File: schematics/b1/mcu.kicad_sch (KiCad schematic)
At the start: 0 parts

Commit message: Added schematic page for the status block.
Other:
- company: (none) -> shawnd.xyz
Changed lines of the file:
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@@
   (title_block
     (title "B1")
-    (date "2024-02-01")
+    (date "2024-02-05")
     (rev "1")
+    (company "shawnd.xyz")
     (comment 2 "scanning as well as radio communications and outputs/displays.")
     (comment 3 "A B1 (Badger One) node is the core hardware unit of the Badger sytem. It handles card")

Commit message: General schematic updates.
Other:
- title: B1 -> (none)
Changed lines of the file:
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@@
   (paper "A4")
   (title_block
-    (title "B1")
     (date "2024-02-06")
     (rev "1")
     (company "shawnd.xyz")
-    (comment 2 "scanning as well as radio communications and outputs/displays.")
-    (comment 3 "A B1 (Badger One) node is the core hardware unit of the Badger sytem. It handles card")
   )
 )

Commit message: Added MCU primary schematic page.
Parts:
- added C17, C19: 22pF, Capacitor_THT:C_Disc_D3.0mm_W1.6mm_P2.50mm, symbol Device:C
- added C21: 0.1u, symbol Device:C
- added C22: 1u, symbol Device:C
- added C23: 10u, symbol Device:C_Polarized
- added Q10, Q11, Q12: 2N3904, Package_TO_SOT_THT:TO-92_Inline, symbol Transistor_BJT:2N3904
- added R31: 10kΩ, Resistor_THT:R_Axial_DIN0204_L3.6mm_D1.6mm_P7.62mm_Horizontal, symbol Device:R
- added R32, R33, R34, R35, R36, R37: 10k, symbol Device:R
- added U9: ATmega328-P, Package_DIP:DIP-28_W7.62mm_Socket, symbol MCU_Microchip_ATmega:ATmega328-P
- added Y1: 16MHz, Crystal:Crystal_HC49-U_Vertical, symbol Device:Crystal
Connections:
- new net: Q10.2 (B), R32.2
- new net: Q11.2 (B), R34.2
- new net: C19.1, U9.10 (XTAL2/PB7), Y1.1
- new net: R31.2, U9.1 (~{RESET}/PC6)
- new net: C17.2, U9.9 (XTAL1/PB6), Y1.2
- new net: Q12.2 (B), R37.2
- new net DIO0: U9.12 (PD6)
- new net GND: C17.1, C19.2, C21.2, C22.2, C23.2, Q10.1 (E), Q11.1 (E), Q12.1 (E), U9.22 (GND), U9.8 (GND)
- new net MISO: U9.18 (PB4)
- new net MOSI: U9.17 (PB3)
- new net RST0: U9.6 (PD4)
- new net SCK: U9.19 (PB5)
- new net TONE: U9.23 (PC0)
- new net VCC: C21.1, C22.1, C23.1, R31.1, R33.2, R35.2, R36.2, U9.20 (AVCC), U9.7 (VCC)
- new net VCC_ISR: Q10.3 (C), R33.1
- new net VCC_LORA: Q12.3 (C), R36.1
- new net VCC_SCAN: Q11.3 (C), R35.1
- new net ~{CS0}: R32.1, U9.16 (PB2)
- new net ~{CS1}: U9.15 (PB1)
- new net ~{CS2}: R34.1, U9.14 (PB0)
- new net ~{CS3}: R37.1, U9.13 (PD7)
- new net ~{PL}: U9.11 (PD5)
- new net ~{RST1}: U9.5 (PD3)
- no-connect marks 0 -> 3

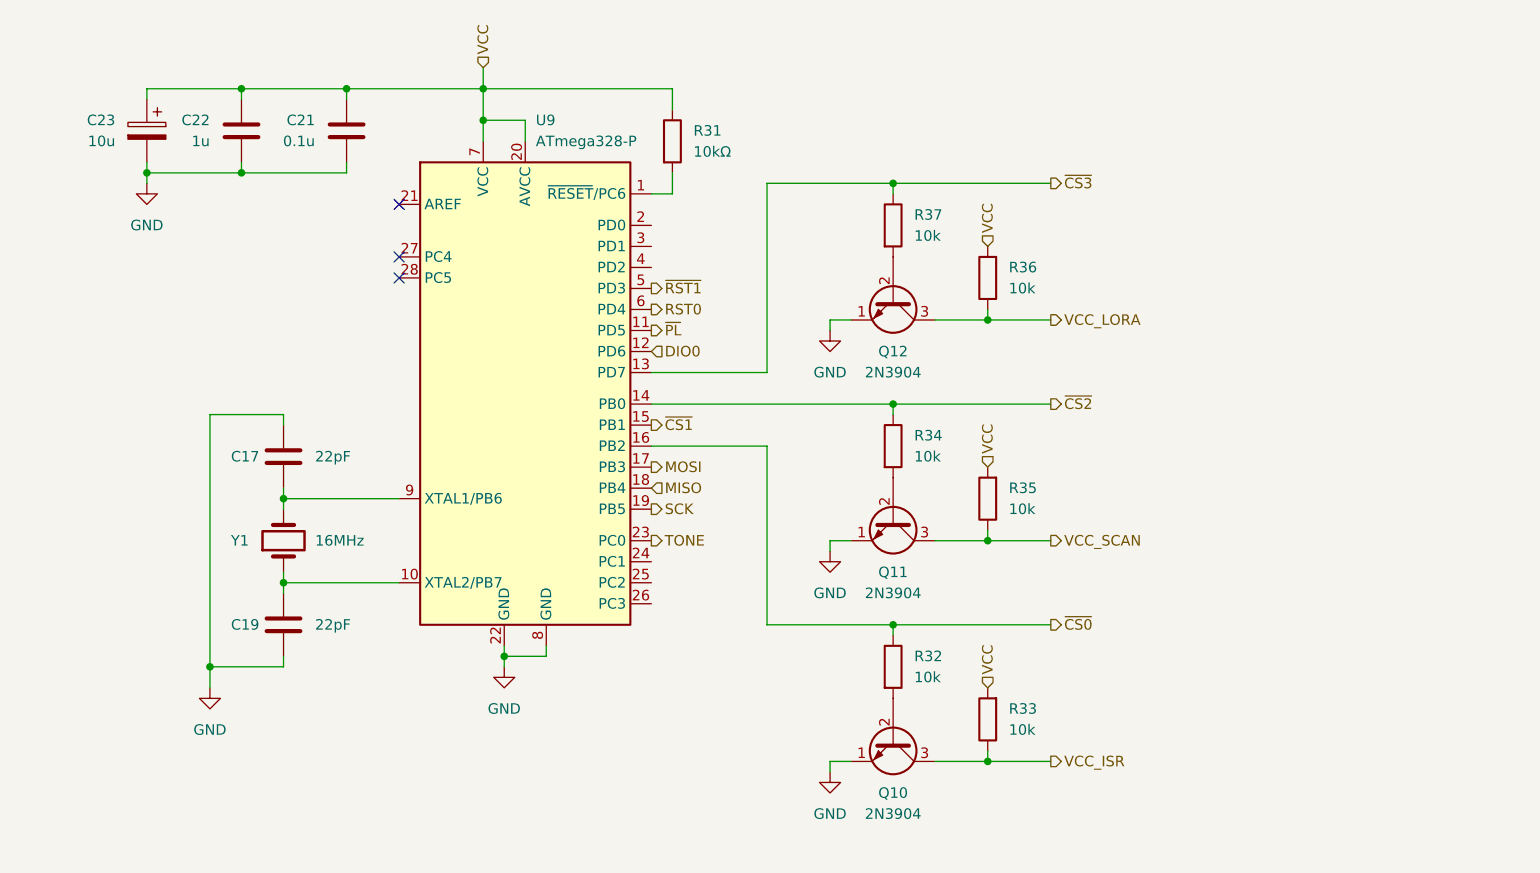
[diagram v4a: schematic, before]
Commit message: Updated MCU and B1 schematic pages.
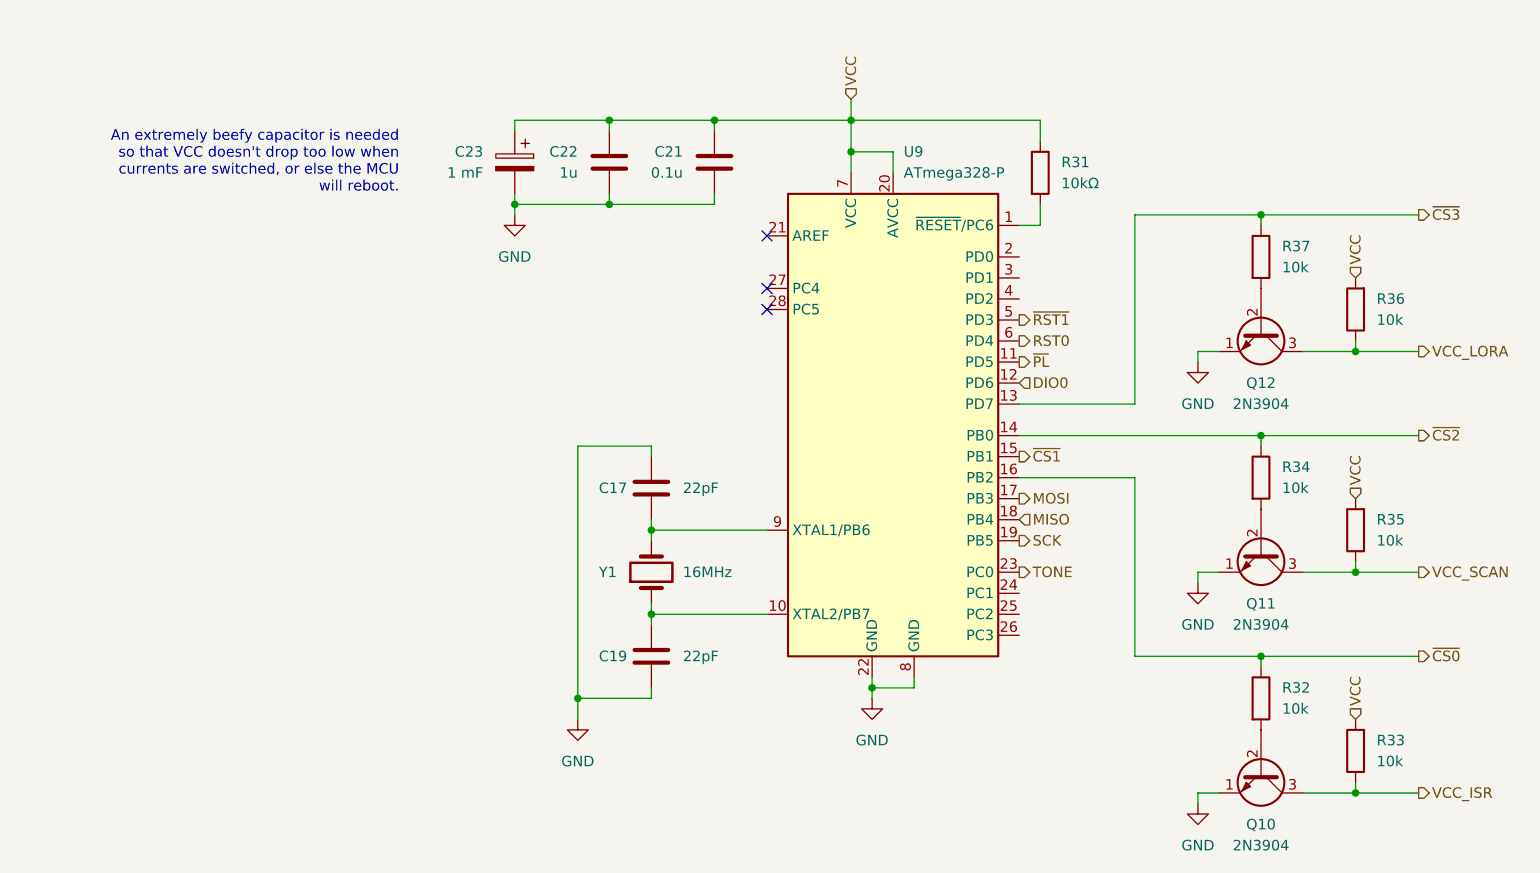
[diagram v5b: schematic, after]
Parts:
- C23: value 10u -> 1 mF
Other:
- note added: "An extremely beefy capacitor is needed so that VCC doesn't drop too low when currents are switched, or else the MCU will reboot."
- moved on the sheet: C17, C19, C21, C22, C23, Q10, Q11, Q12, R31, R32, R33, R34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

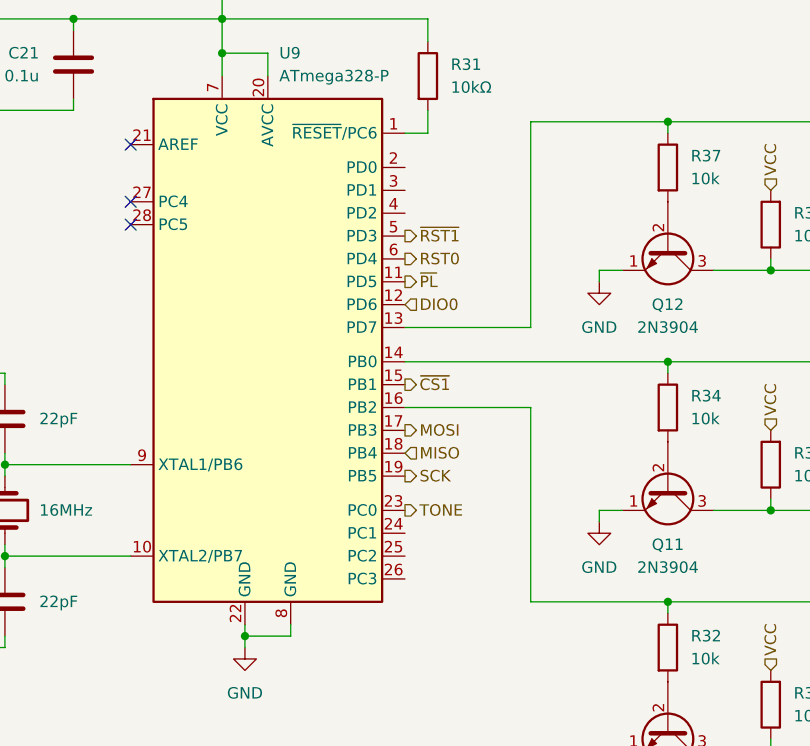
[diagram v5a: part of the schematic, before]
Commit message: Updated MCU and B1 schematics.
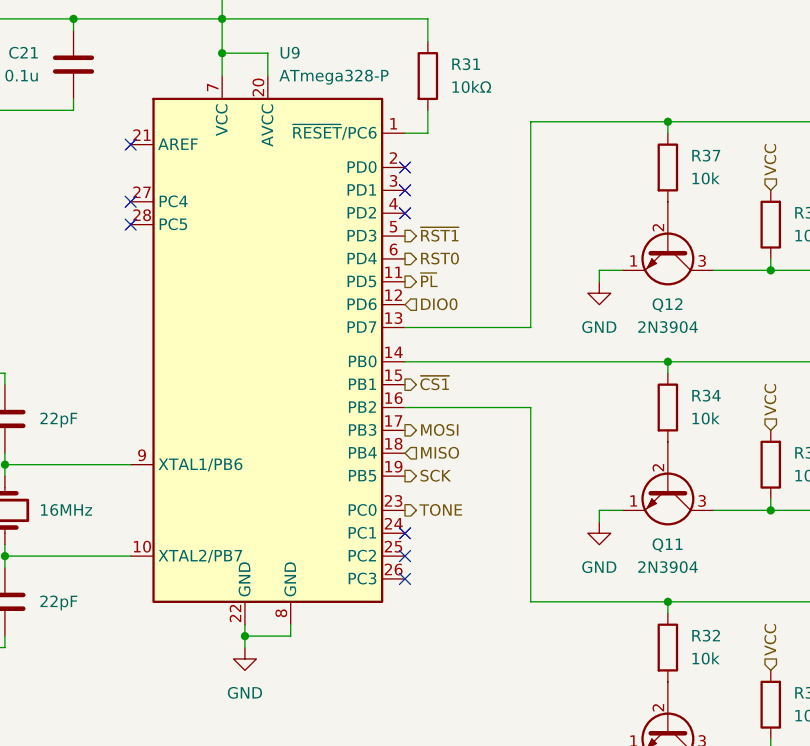
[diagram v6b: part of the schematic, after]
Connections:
- no-connect marks 3 -> 9
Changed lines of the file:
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@@
   )
   (no_connect (at 128.27 59.69))
+  (no_connect (at 158.75 107.95))
+  (no_connect (at 158.75 105.41))
+  (no_connect (at 158.75 102.87))
   (no_connect (at 128.27 68.58))
+  (no_connect (at 158.75 62.23))
+  (no_connect (at 158.75 67.31))
   (no_connect (at 128.27 66.04))
+  (no_connect (at 158.75 64.77))
   (wire (pts (xy 161.29 58.42) (xy 161.29 55.88))
     (stroke (width 0) (type default))

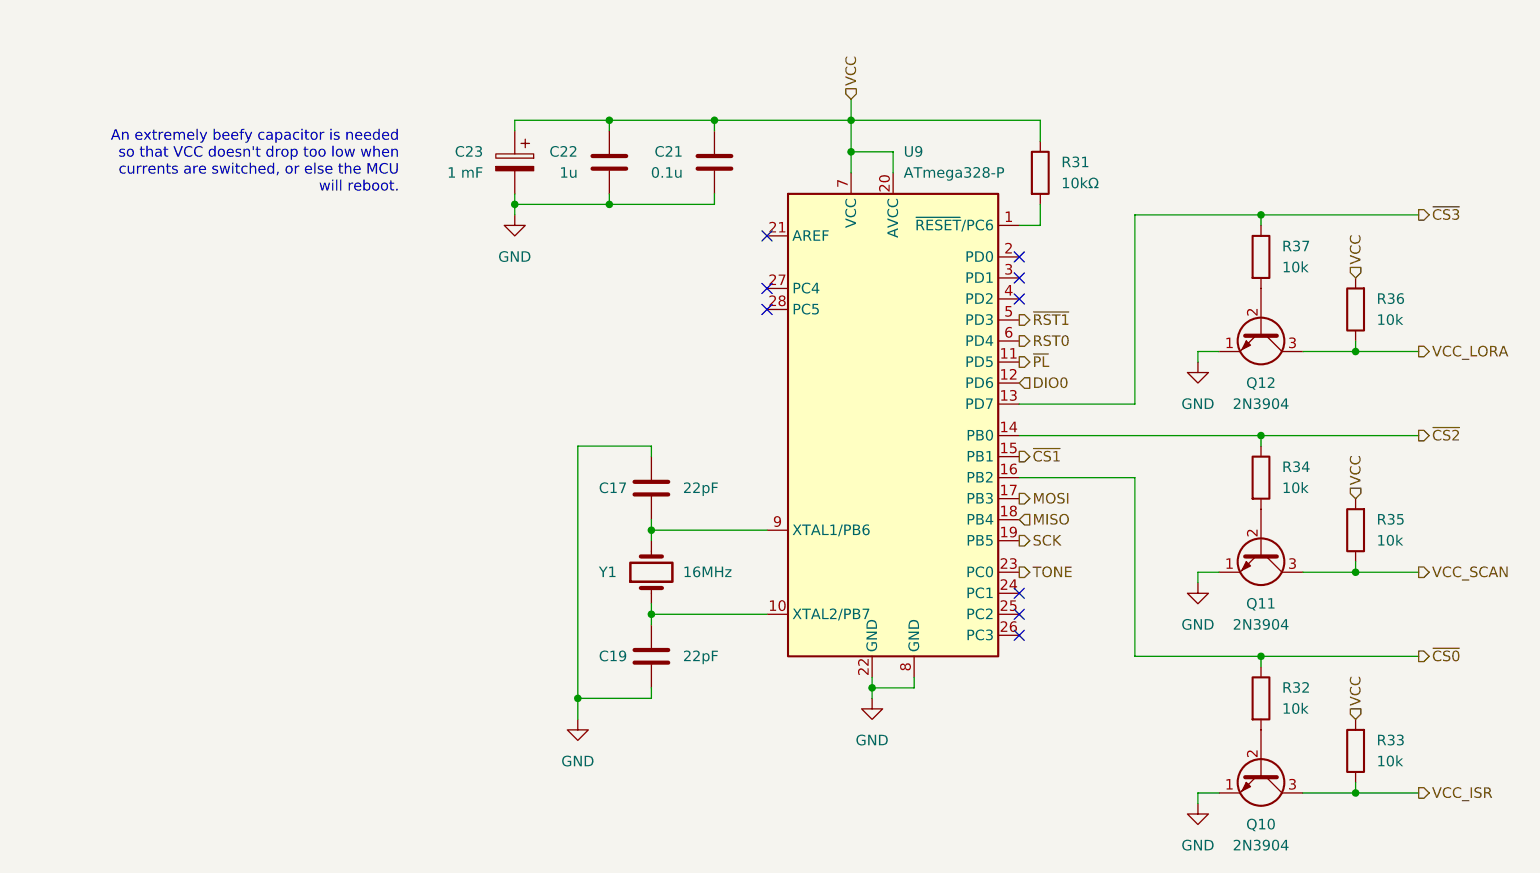
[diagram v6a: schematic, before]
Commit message: Changed tone pin.
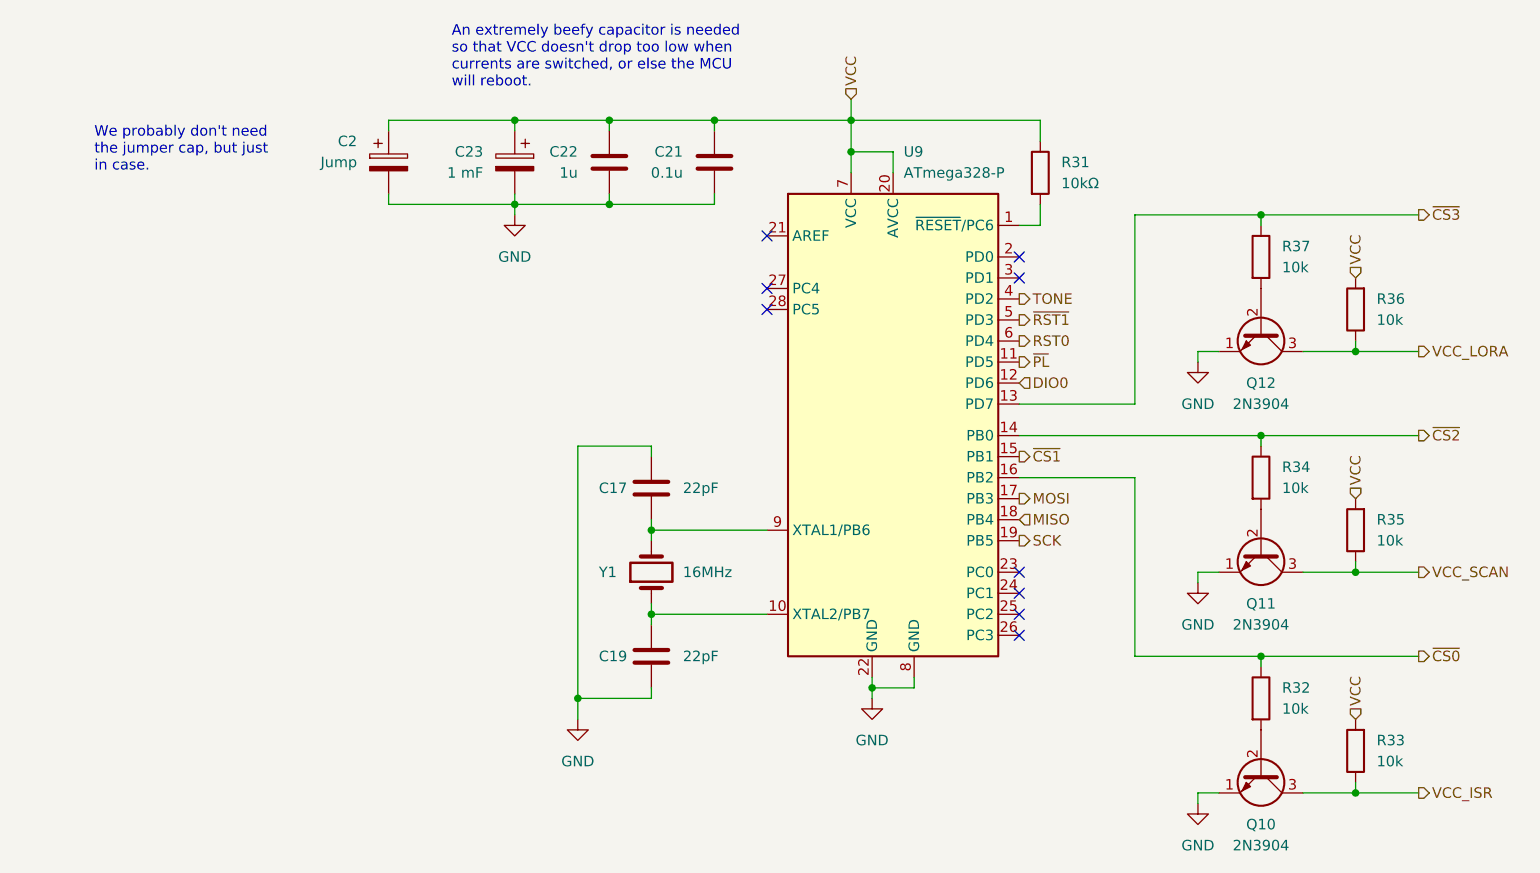
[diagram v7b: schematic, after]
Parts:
- added C2: Jump, symbol Device:C_Polarized
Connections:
- net GND: now also C2.2
- net TONE: now also U9.4 (PD2); no longer U9.23 (PC0)
- net VCC: now also C2.1
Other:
- note added: "We probably don't need the jumper cap, but just in case."
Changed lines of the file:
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@@
   (junction (at 109.22 55.88) (diameter 0) (color 0 0 0 0)
+  )
+  (junction (at 97.79 45.72) (diameter 0) (color 0 0 0 0)
   )
   (junction (at 140.97 114.3) (diameter 0) (color 0 0 0 0)
@@
   (no_connect (at 158.75 105.41))
   (no_connect (at 158.75 102.87))
+  (no_connect (at 158.75 100.33))
   (no_connect (at 128.27 68.58))
   (no_connect (at 158.75 62.23))
-  (no_connect (at 158.75 67.31))
   (no_connect (at 128.27 66.04))
   (no_connect (at 158.75 64.77))
+  (wire (pts (xy 82.55 55.88) (xy 82.55 54.61))
+    (stroke (width 0) (type default))
+  )
   (wire (pts (xy 161.29 58.42) (xy 161.29 55.88))
     (stroke (width 0) (type default))
@@
     (stroke (width 0) (type default))
   )
+  (wire (pts (xy 97.79 54.61) (xy 97.79 55.88))
+    (stroke (width 0) (type default))
+  )
   (wire (pts (xy 182.88 127) (xy 180.34 127))
     (stroke (width 0) (type default))
@@
     (stroke (width 0) (type default))
   )
-  (wire (pts (xy 97.79 54.61) (xy 97.79 55.88))
-    (stroke (width 0) (type default))
-  )
   (wire (pts (xy 121.92 45.72) (xy 138.43 45.72))
     (stroke (width 0) (type default))
   )
+  (wire (pts (xy 97.79 45.72) (xy 82.55 45.72))
+    (stroke (width 0) (type default))
+  )
   (wire (pts (xy 109.22 46.99) (xy 109.22 45.72))
     (stroke (width 0) (type default))
@@
     (stroke (width 0) (type default))
   )
+  (wire (pts (xy 82.55 55.88) (xy 97.79 55.88))
+    (stroke (width 0) (type default))
+  )
   (wire (pts (xy 199.39 99.06) (xy 199.39 100.33))
     (stroke (width 0) (type default))
@@
     (stroke (width 0) (type default))
   )
+  (wire (pts (xy 82.55 45.72) (xy 82.55 46.99))
+    (stroke (width 0) (type default))
+  )
   (wire (pts (xy 207.01 127) (xy 199.39 127))
     (stroke (width 0) (type default))
@@
   )
   (text "An extremely beefy capacitor is needed\nso that VCC doesn't drop too low when\ncurrents are switched, or else the MCU\nwill reboot."
-    (at 83.82 54.61 0)
-    (effects (font (size 1.27 1.27)) (justify right bottom))
-  )
-  (hierarchical_label "TONE" (shape output) (at 158.75 100.33 0) (fields_autoplaced)
-    (effects (font (size 1.27 1.27)) (justify left))
+    (at 90.17 41.91 0)
+    (effects (font (size 1.27 1.27)) (justify left bottom))
+  )
+  (text "We probably don't need\nthe jumper cap, but just\nin case."
+    (at 46.99 52.07 0)
+    (effects (font (size 1.27 1.27)) (justify left bottom))
   )
   (hierarchical_label "DIO0" (shape input) (at 158.75 77.47 0) (fields_autoplaced)
@@
   )
   (hierarchical_label "VCC" (shape input) (at 199.39 64.77 90) (fields_autoplaced)
+    (effects (font (size 1.27 1.27)) (justify left))
+  )
+  (hierarchical_label "TONE" (shape output) (at 158.75 67.31 0) (fields_autoplaced)
     (effects (font (size 1.27 1.27)) (justify left))
   )
@@
         )
       )
+    )
+  )
+  (symbol (lib_id "Device:C_Polarized") (at 82.55 50.8 0) (unit 1)
+    (in_bom yes) (on_board yes) (dnp no)
+    (property "Reference" "C2" (at 78.74 48.26 0)
+      (effects (font (size 1.27 1.27)) (justify right))
+    )
+    (property "Value" "Jump" (at 78.74 50.8 0)
+      (effects (font (size 1.27 1.27)) (justify right))
+    )
+    (property "Footprint" "" (at 83.5152 54.61 0)
+      (effects (font (size 1.27 1.27)) hide)
+    )
+    (property "Datasheet" "~" (at 82.55 50.8 0)
+      (effects (font (size 1.27 1.27)) hide)
+    )
+    (pin "2")
+    (pin "1")
+    (instances
+      (project "b1"
+        (path "/d6142fa5-2354-4512-9919-37616259c364/c54abc85-6b3c-456e-a8eb-1ec3c5617327"
+          (reference "C2") (unit 1)
+        )
+      )

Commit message: Updated annotations.
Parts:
- renumbered C2 to C11, C23 to C12, C22 to C13, C17 to C14, C19 to C15, C21 to C16, Q12 to Q2, Q11 to Q3, Q10 to Q4, R31 to R22, R37 to R23, R34 to R24, R32 to R25, R36 to R26, R35 to R27, R33 to R28, U9 to U7
